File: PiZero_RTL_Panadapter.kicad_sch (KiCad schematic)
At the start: 22 parts, among them J1 Conn_01x02, J2 JST GH 8 Position, J3 U.FL, J4 U.FL, J5 Conn_01x08, T1 DXW21BN2511NL, U1 RPM5.0-2.0, U2 AP2114HA-3.3, U4 Raspberry Pi Zero 2W

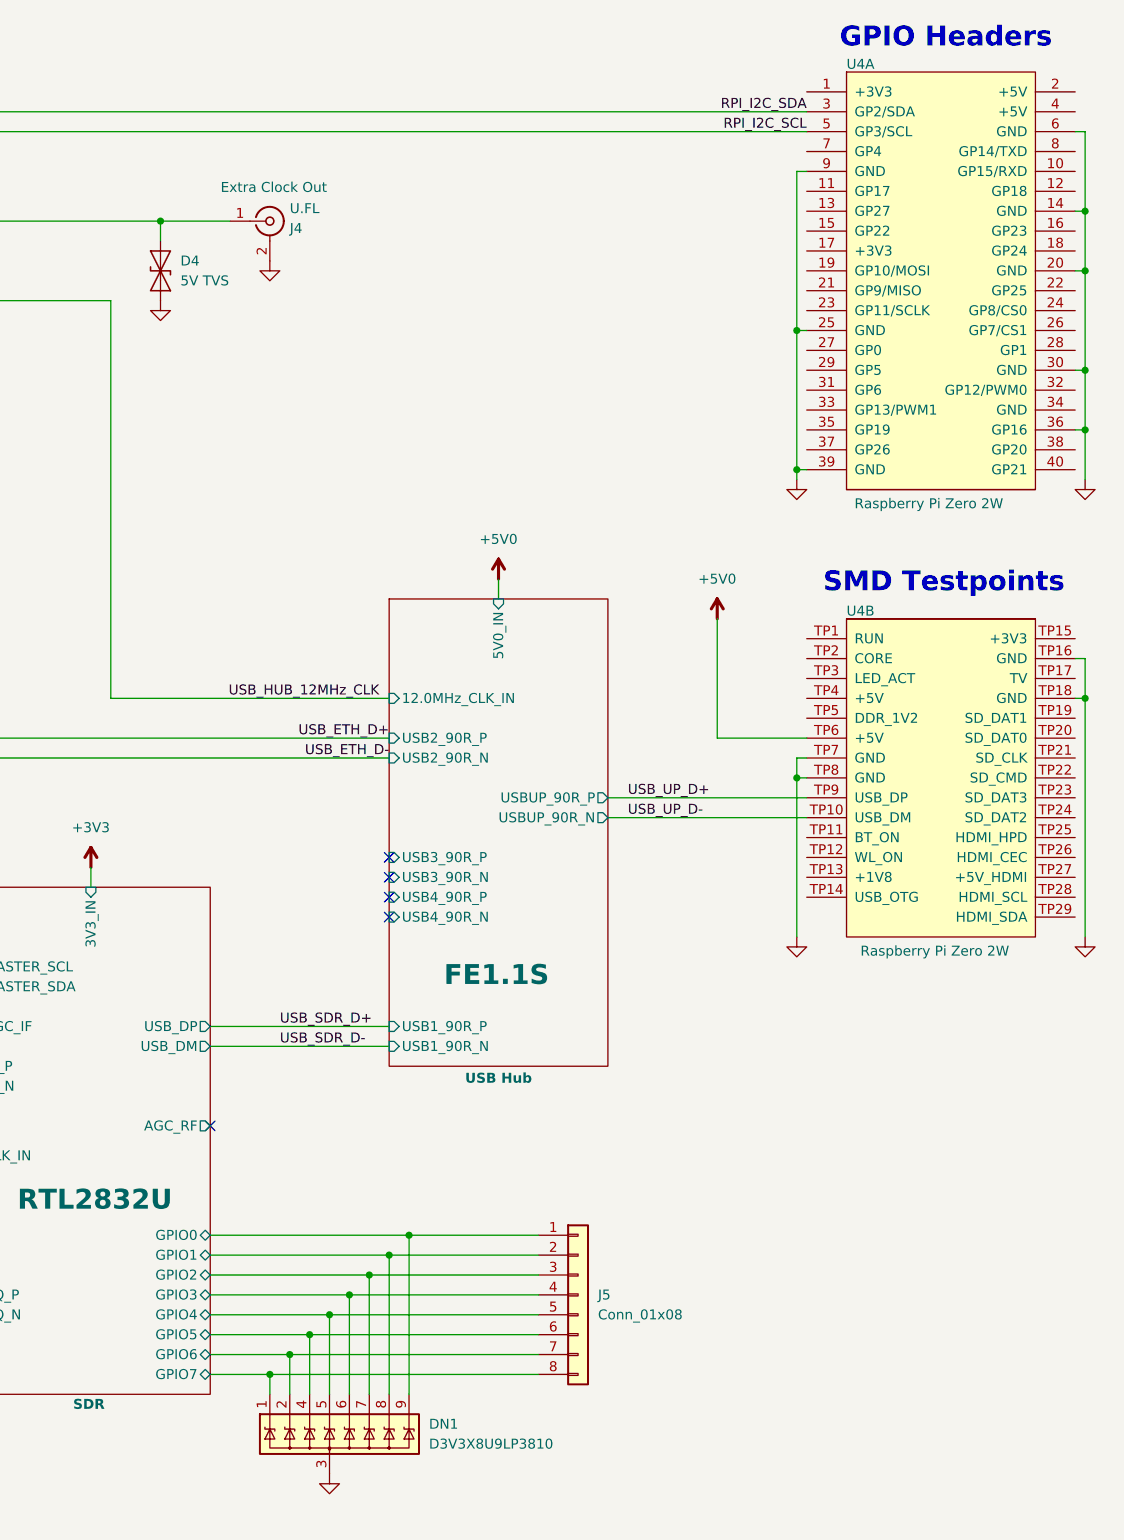
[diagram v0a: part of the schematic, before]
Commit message: PCB Routing Complete
On to silkscreen...
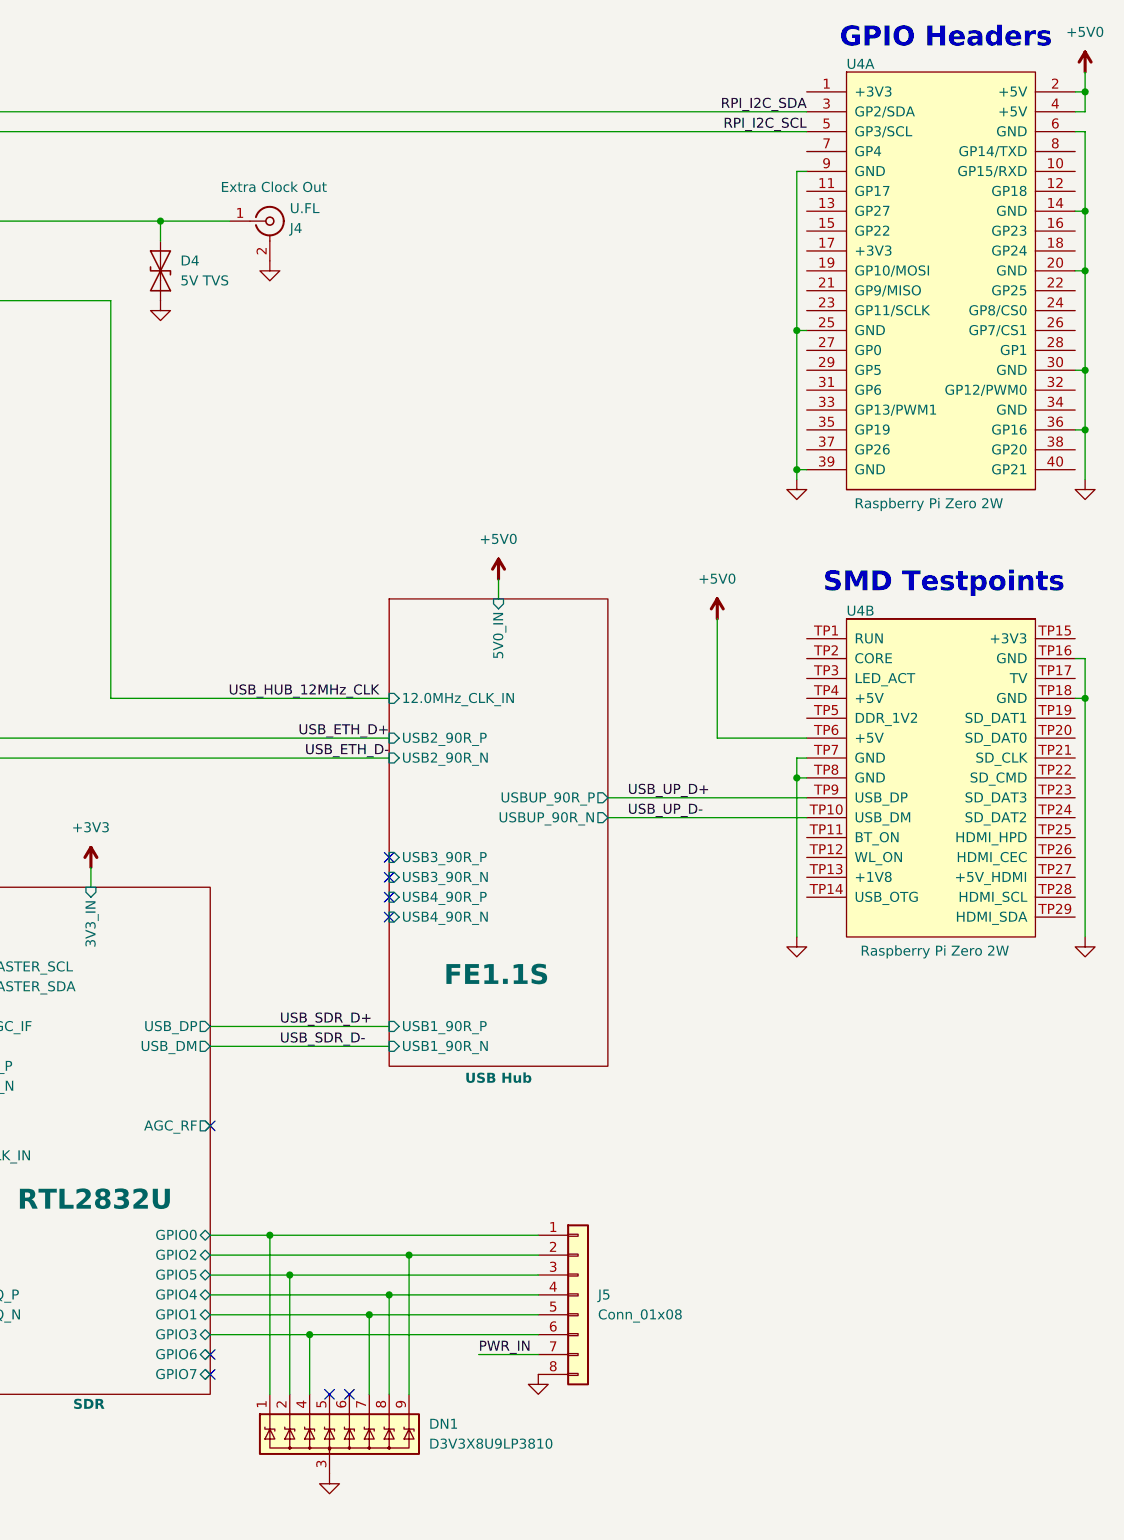
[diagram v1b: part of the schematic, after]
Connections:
- net +5V0: now also U4.2 (+5V), U4.4 (+5V)
- net GND: now also J5.8 (Pin_8)
- net PWR_IN: now also J5.7 (Pin_7)
- net SDR/GPIO0: now also DN1.1 (Line-1); no longer DN1.9 (Line-2)
- net SDR/GPIO1: now also DN1.7 (Line-5), J5.5 (Pin_5); no longer DN1.8 (Line-4), J5.2 (Pin_2)
- net SDR/GPIO2: now also DN1.9 (Line-2), J5.2 (Pin_2); no longer DN1.7 (Line-5), J5.3 (Pin_3)
- net SDR/GPIO3: now also DN1.4 (Line-6), J5.6 (Pin_6); no longer DN1.6 (Line-7), J5.4 (Pin_4)
- net SDR/GPIO4: now also DN1.8 (Line-4), J5.4 (Pin_4); no longer DN1.5 (Line-8), J5.5 (Pin_5)
- net SDR/GPIO5: now also DN1.2 (Line-3), J5.3 (Pin_3); no longer DN1.4 (Line-6), J5.6 (Pin_6)
- net SDR/GPIO6: no longer DN1.2 (Line-3), J5.7 (Pin_7)
- net SDR/GPIO7: no longer DN1.1 (Line-1), J5.8 (Pin_8)
- no-connect marks 8 -> 12
